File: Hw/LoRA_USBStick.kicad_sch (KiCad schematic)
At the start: 37 parts, among them J10 USB_B, J4 SWD, SW1 RST, SW2 BOOT, SW3 RST, U1 RP2040, U2 RFM95W-868S2, U3 AP2112K-3.3, U4 W25Q16JV, Y1 12Mhz

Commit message: change button for jumper force jumper
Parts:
- removed R1: 1K, Resistor_SMD:R_0603_1608Metric, symbol Device:R_Small
- removed SW2: BOOT, Button_Switch_SMD:SW_SPST_TL3342, symbol Switch:SW_Push
- added JP?: BOOT, symbol Jumper:Jumper_2_Open
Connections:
- net GND: now also JP?.1 (A)
- net QSPI_CS: now also JP?.2 (B)
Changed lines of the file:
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@@
-    (stroke (width 0) (type default) (color 0 0 0 0))
-  )
-  (wire (pts (xy 63.119 129.54) (xy 66.675 129.54))
     (stroke (width 0) (type default) (color 0 0 0 0))
   )
@@
     (stroke (width 0) (type default) (color 0 0 0 0))
   )
-  (wire (pts (xy 50.038 129.54) (xy 50.038 130.556))
+  (wire (pts (xy 55.118 113.03) (xy 55.118 114.046))
     (stroke (width 0) (type default) (color 0 0 0 0))
   )
@@
     (stroke (width 0) (type default) (color 0 0 0 0))
   )
-  (wire (pts (xy 71.755 129.54) (xy 80.01 129.54))
+  (wire (pts (xy 68.199 113.03) (xy 76.454 113.03))
     (stroke (width 0) (type default) (color 0 0 0 0))
   )
@@
     (stroke (width 0) (type default) (color 0 0 0 0))
   )
-  (wire (pts (xy 52.959 129.54) (xy 50.038 129.54))
+  (wire (pts (xy 58.039 113.03) (xy 55.118 113.03))
     (stroke (width 0) (type default) (color 0 0 0 0))
   )
@@
     (effects (font (size 1.27 1.27)) (justify right bottom))
   )
-  (label "QSPI_CS" (at 80.01 129.54 0)
+  (label "QSPI_CS" (at 76.454 113.03 0)
     (effects (font (size 1.27 1.27)) (justify left bottom))
   )
@@
     (pin "2")
   )
-  (symbol (lib_id "Device:R_Small") (at 69.215 129.54 270) (unit 1)
-    (in_bom yes) (on_board yes)
-    (property "Reference" "R1" (id 0) (at 69.215 124.5616 90))
-    (property "Value" "1K" (id 1) (at 69.215 126.873 90))
-    (property "Footprint" "Resistor_SMD:R_0603_1608Metric" (id 2) (at 69.215 129.54 0)
-      (effects (font (size 1.27 1.27)) hide)
-    )
-    (property "Datasheet" "https://lcsc.com/product-detail/Chip-Resistor-Surface-Mount_Walsin-Tech-Corp-Walsin-Tech-Corp-1KR-102-5_C384390.html" (id 3) (at 69.215 129.54 0)
-      (effects (font (size 1.27 1.27)) hide)
-    )
-    (property "LCSC#" "" (id 4) (at 69.215 129.54 0)
-      (effects (font (size 1.27 1.27)) hide)
-    )
-    (property "manf#" "" (id 5) (at 69.215 129.54 0)
-      (effects (font (size 1.27 1.27)) hide)
-    )
-    (pin "1")
-    (pin "2")
-  )
   (symbol (lib_id "power:+1V2") (at 116.332 144.018 0) (unit 1)
     (in_bom yes) (on_board yes)
@@
     (pin "1")
   )
-  (symbol (lib_id "power:GND") (at 50.038 130.556 0) (unit 1)
-    (in_bom yes) (on_board yes)
-    (property "Reference" "#PWR02" (id 0) (at 50.038 136.906 0)
-      (effects (font (size 1.27 1.27)) hide)
-    )
-    (property "Value" "GND" (id 1) (at 50.165 134.9502 0))
-    (property "Footprint" "" (id 2) (at 50.038 130.556 0)
-      (effects (font (size 1.27 1.27)) hide)
-    )
-    (property "Datasheet" "" (id 3) (at 50.038 130.556 0)
+  (symbol (lib_id "power:GND") (at 55.118 114.046 0) (unit 1)
+    (in_bom yes) (on_board yes)
+    (property "Reference" "#PWR02" (id 0) (at 55.118 120.396 0)
+      (effects (font (size 1.27 1.27)) hide)
+    )
+    (property "Value" "GND" (id 1) (at 55.245 118.4402 0))
+    (property "Footprint" "" (id 2) (at 55.118 114.046 0)
+      (effects (font (size 1.27 1.27)) hide)
+    )
+    (property "Datasheet" "" (id 3) (at 55.118 114.046 0)
       (effects (font (size 1.27 1.27)) hide)
     )
@@
     (pin "1")
   )
-  (symbol (lib_id "Switch:SW_Push") (at 58.039 129.54 0) (unit 1)
-    (in_bom yes) (on_board yes)
-    (property "Reference" "SW2" (id 0) (at 58.039 122.301 0))
-    (property "Value" "BOOT" (id 1) (at 58.039 124.6124 0))
-    (property "Footprint" "Button_Switch_SMD:SW_SPST_TL3342" (id 2) (at 58.039 124.46 0)
-      (effects (font (size 1.27 1.27)) hide)
-    )
-    (property "Datasheet" "https://lcsc.com/product-detail/Tactile-Switches_XUNPU-TS-1088R-02526_C455281.html" (id 3) (at 58.039 124.46 0)
-      (effects (font (size 1.27 1.27)) hide)
-    )
-    (property "LCSC#" "" (id 4) (at 58.039 129.54 0)
-      (effects (font (size 1.27 1.27)) hide)
-    )
-    (property "manf#" "TS-1088R-02526" (id 5) (at 58.039 129.54 0)
-      (effects (font (size 1.27 1.27)) hide)
-    )
-    (pin "1")
-    (pin "2")
-  )
   (symbol (lib_id "Device:C_Small") (at 140.97 147.828 0) (unit 1)
     (in_bom yes) (on_board yes)
@@
     )
     (pin "1")
+  )
+  (symbol (lib_id "Jumper:Jumper_2_Open") (at 63.119 113.03 0) (unit 1)
+    (in_bom yes) (on_board yes) (fields_autoplaced)
+    (property "Reference" "JP?" (id 0) (at 63.119 106.68 0))
+    (property "Value" "BOOT" (id 1) (at 63.119 109.22 0))
+    (property "Footprint" "" (id 2) (at 63.119 113.03 0)
+      (effects (font (size 1.27 1.27)) hide)
+    )
+    (property "Datasheet" "~" (id 3) (at 63.119 113.03 0)
+      (effects (font (size 1.27 1.27)) hide)
+    )
+    (pin "1")
+    (pin "2")
   )
   (symbol (lib_id "power:+3V3") (at 155.956 144.272 0) (unit 1)
@@
       (reference "J10") (unit 1) (value "USB_B") (footprint "Connectors:C46394")
     )
-    (path "/73f553b6-40ee-427d-ad00-5afb150dad9e"
-      (reference "R1") (unit 1) (value "1K") (footprint "Resistor_SMD:R_0603_1608Metric")
+    (path "/d9378caf-b15d-41bb-9a08-9c338c99bca0"
+      (reference "JP?") (unit 1) (value "BOOT") (footprint "")
     )
     (path "/f60959af-078b-4b94-af6b-240a70c175cf"
@@
       (reference "SW1") (unit 1) (value "RST") (footprint "Button_Switch_SMD:SW_SPST_TL3342")
     )
-    (path "/9de120ec-a78c-4e0b-898c-8bcfaa48c96b"
-      (reference "SW2") (unit 1) (value "BOOT") (footprint "Button_Switch_SMD:SW_SPST_TL3342")
-    )
     (path "/bd279f0b-459f-41ba-8171-ac9414a30ac1"

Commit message: Place footprints on the PCB
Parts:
- removed SW1: RST, Button_Switch_SMD:SW_SPST_TL3342, symbol LoRA_USBStick-rescue:SW_Push
- JP1: renamed from JP?; footprint (none) -> Jumper:SolderJumper-2_P1.3mm_Open_Pad1.0x1.5mm
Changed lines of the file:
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@@
-    (stroke (width 0) (type default) (color 0 0 0 0))
-  )
-  (wire (pts (xy 163.83 173.99) (xy 163.83 176.53))
     (stroke (width 0) (type default) (color 0 0 0 0))
   )
@@
   )
   (polyline (pts (xy 63.881 197.993) (xy 63.881 166.116))
-    (stroke (width 0) (type default) (color 0 0 0 0))
-  )
-  (wire (pts (xy 163.83 187.833) (xy 163.83 186.69))
     (stroke (width 0) (type default) (color 0 0 0 0))
   )
@@
     (effects (font (size 1.27 1.27)) (justify left bottom))
   )
-  (label "RST" (at 163.83 173.99 0)
-    (effects (font (size 1.524 1.524)) (justify left bottom))
-  )
   (label "MISO" (at 233.68 29.21 180)
     (effects (font (size 1.524 1.524)) (justify right bottom))
@@
   (label "QSPI_DATA3" (at 268.732 148.59 0)
     (effects (font (size 1.27 1.27)) (justify left bottom))
-  )
-  (symbol (lib_id "LoRA_USBStick-rescue:SW_Push") (at 163.83 181.61 270) (unit 1)
-    (in_bom yes) (on_board yes)
-    (property "Reference" "SW1" (id 0) (at 166.37 182.88 0)
-      (effects (font (size 1.27 1.27)) (justify left))
-    )
-    (property "Value" "RST" (id 1) (at 162.306 181.61 0))
-    (property "Footprint" "Button_Switch_SMD:SW_SPST_TL3342" (id 2) (at 168.91 181.61 0)
-      (effects (font (size 1.27 1.27)) hide)
-    )
-    (property "Datasheet" "" (id 3) (at 168.91 181.61 0)
-      (effects (font (size 1.27 1.27)) hide)
-    )
-    (property "manf#" "B3U-1000P" (id 4) (at 163.83 181.61 0)
-      (effects (font (size 1.524 1.524)) hide)
-    )
-    (pin "1")
-    (pin "2")
-  )
-  (symbol (lib_id "power:GND") (at 163.83 187.833 0) (unit 1)
-    (in_bom yes) (on_board yes)
-    (property "Reference" "#PWR01" (id 0) (at 163.83 194.183 0)
-      (effects (font (size 1.27 1.27)) hide)
-    )
-    (property "Value" "GND" (id 1) (at 163.83 191.643 0))
-    (property "Footprint" "" (id 2) (at 163.83 187.833 0)
-      (effects (font (size 1.27 1.27)) hide)
-    )
-    (property "Datasheet" "" (id 3) (at 163.83 187.833 0)
-      (effects (font (size 1.27 1.27)) hide)
-    )
-    (pin "1")
   )
   (symbol (lib_id "power:+3.3V") (at 270.129 25.908 0) (unit 1)
@@
   (symbol (lib_id "power:+3V3") (at 142.24 173.736 0) (unit 1)
     (in_bom yes) (on_board yes)
-    (property "Reference" "#PWR?" (id 0) (at 142.24 177.546 0)
+    (property "Reference" "#PWR0101" (id 0) (at 142.24 177.546 0)
       (effects (font (size 1.27 1.27)) hide)
     )
@@
   (symbol (lib_id "power:GND") (at 140.208 187.325 0) (unit 1)
     (in_bom yes) (on_board yes)
-    (property "Reference" "#PWR?" (id 0) (at 140.208 193.675 0)
+    (property "Reference" "#PWR0102" (id 0) (at 140.208 193.675 0)
       (effects (font (size 1.27 1.27)) hide)
     )
@@
   (symbol (lib_id "Jumper:Jumper_2_Open") (at 63.119 113.03 0) (unit 1)
     (in_bom yes) (on_board yes) (fields_autoplaced)
-    (property "Reference" "JP?" (id 0) (at 63.119 106.68 0))
+    (property "Reference" "JP1" (id 0) (at 63.119 106.68 0))
     (property "Value" "BOOT" (id 1) (at 63.119 109.22 0))
-    (property "Footprint" "" (id 2) (at 63.119 113.03 0)
+    (property "Footprint" "Jumper:SolderJumper-2_P1.3mm_Open_Pad1.0x1.5mm" (id 2) (at 63.119 113.03 0)
       (effects (font (size 1.27 1.27)) hide)
     )
@@
   )
   (symbol_instances
-    (path "/00000000-0000-0000-0000-00005ae4bbf8"
-      (reference "#PWR01") (unit 1) (value "GND") (footprint "")
-    )
     (path "/98cce9f8-8131-4462-bc8b-bd7b4a579405"
       (reference "#PWR02") (unit 1) (value "GND") (footprint "")
@@
     )
     (path "/24088d74-4964-4661-8abf-71a100aa1a44"
-      (reference "#PWR?") (unit 1) (value "+3V3") (footprint "")
+      (reference "#PWR0101") (unit 1) (value "+3V3") (footprint "")
     )
     (path "/cbc339a4-c9ad-4f29-afcf-8e7d53f29096"
-      (reference "#PWR?") (unit 1) (value "GND") (footprint "")
+      (reference "#PWR0102") (unit 1) (value "GND") (footprint "")
     )
     (path "/00000000-0000-0000-0000-00005b06dd9b"
@@
     )
     (path "/d9378caf-b15d-41bb-9a08-9c338c99bca0"
-      (reference "JP?") (unit 1) (value "BOOT") (footprint "")
+      (reference "JP1") (unit 1) (value "BOOT") (footprint "Jumper:SolderJumper-2_P1.3mm_Open_Pad1.0x1.5mm")
     )
     (path "/f60959af-078b-4b94-af6b-240a70c175cf"
@@
       (reference "R11") (unit 1) (value "120R") (footprint "Resistor_SMD:R_0805_2012Metric_Pad1.15x1.40mm_HandSolder")
     )
-    (path "/00000000-0000-0000-0000-00005ae4bb13"
-      (reference "SW1") (unit 1) (value "RST") (footprint "Button_Switch_SMD:SW_SPST_TL3342")
-    )
     (path "/bd279f0b-459f-41ba-8171-ac9414a30ac1"

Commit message: add footprint memory flash
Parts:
- U4: footprint Package_SO:SOIC-8_5.275x5.275mm_P1.27mm -> RP2040:W25Q16JVUUIQ
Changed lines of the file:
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@@
     (property "Reference" "U4" (id 0) (at 245.872 134.366 0))
     (property "Value" "W25Q16JV" (id 1) (at 260.096 134.112 0))
-    (property "Footprint" "Package_SO:SOIC-8_5.275x5.275mm_P1.27mm" (id 2) (at 252.73 143.51 0)
+    (property "Footprint" "RP2040:W25Q16JVUUIQ" (id 2) (at 252.73 143.51 0)
       (effects (font (size 1.27 1.27)) hide)
     )
@@
     )
     (path "/fadc1c63-6a60-4896-9b12-60b8b11e379e"
-      (reference "U4") (unit 1) (value "W25Q16JV") (footprint "Package_SO:SOIC-8_5.275x5.275mm_P1.27mm")
+      (reference "U4") (unit 1) (value "W25Q16JV") (footprint "RP2040:W25Q16JVUUIQ")
     )
     (path "/14b1cf47-fbe7-4d12-9fae-81e256db3a7b"

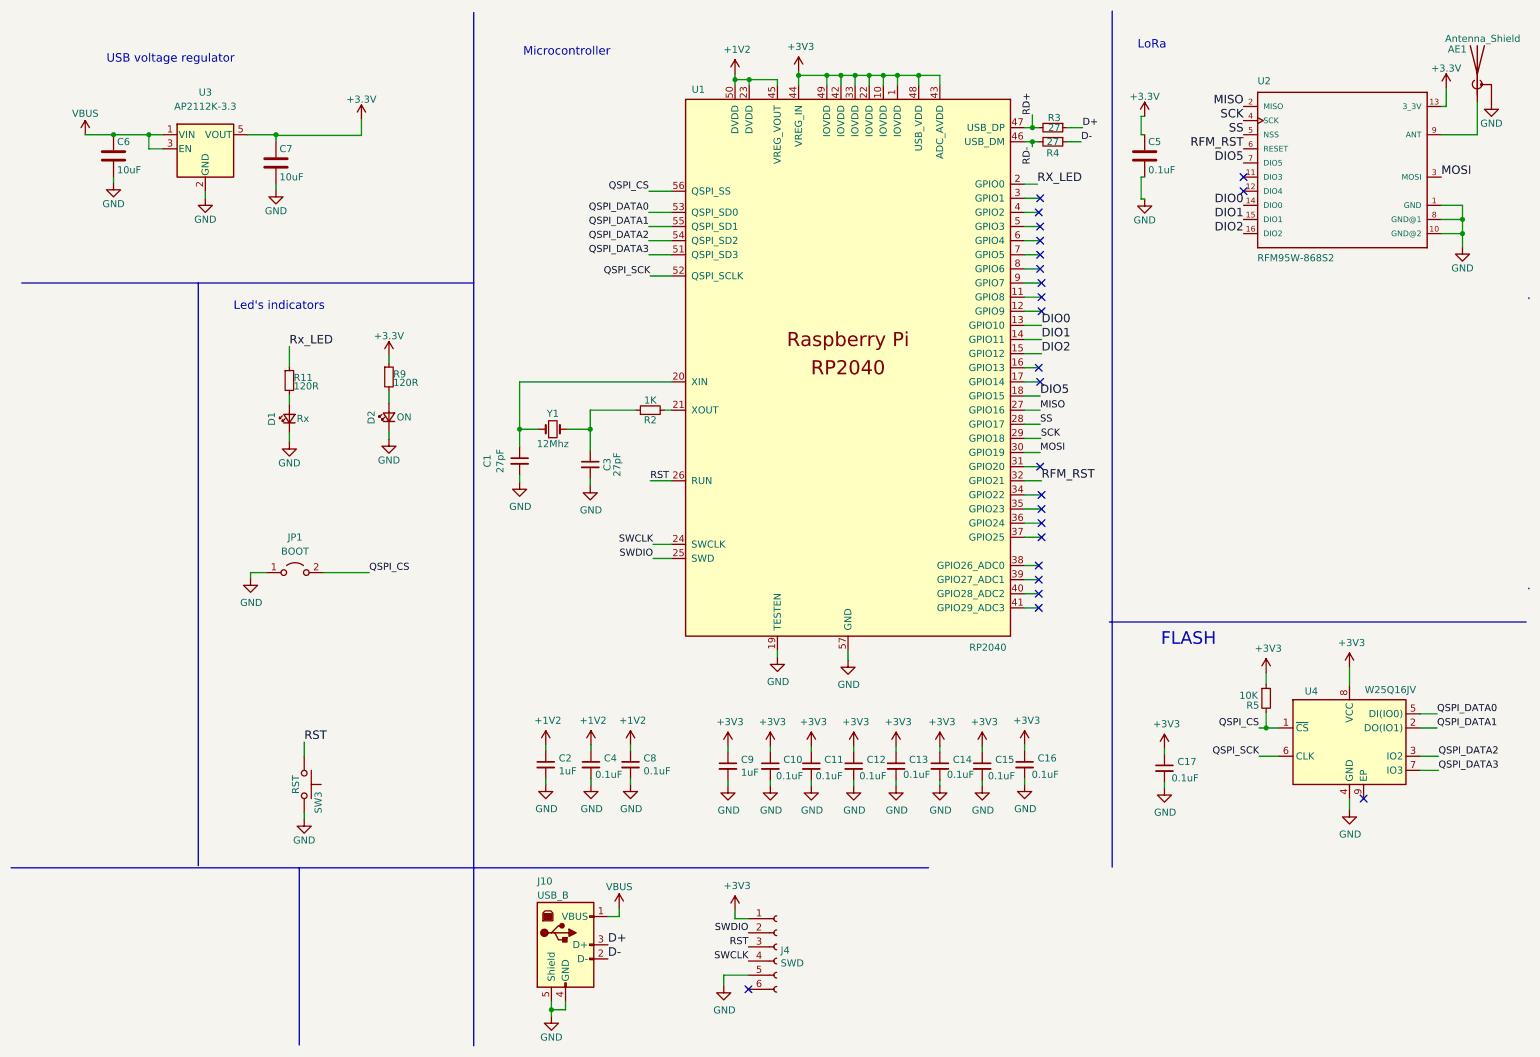
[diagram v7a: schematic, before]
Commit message: New floor plan
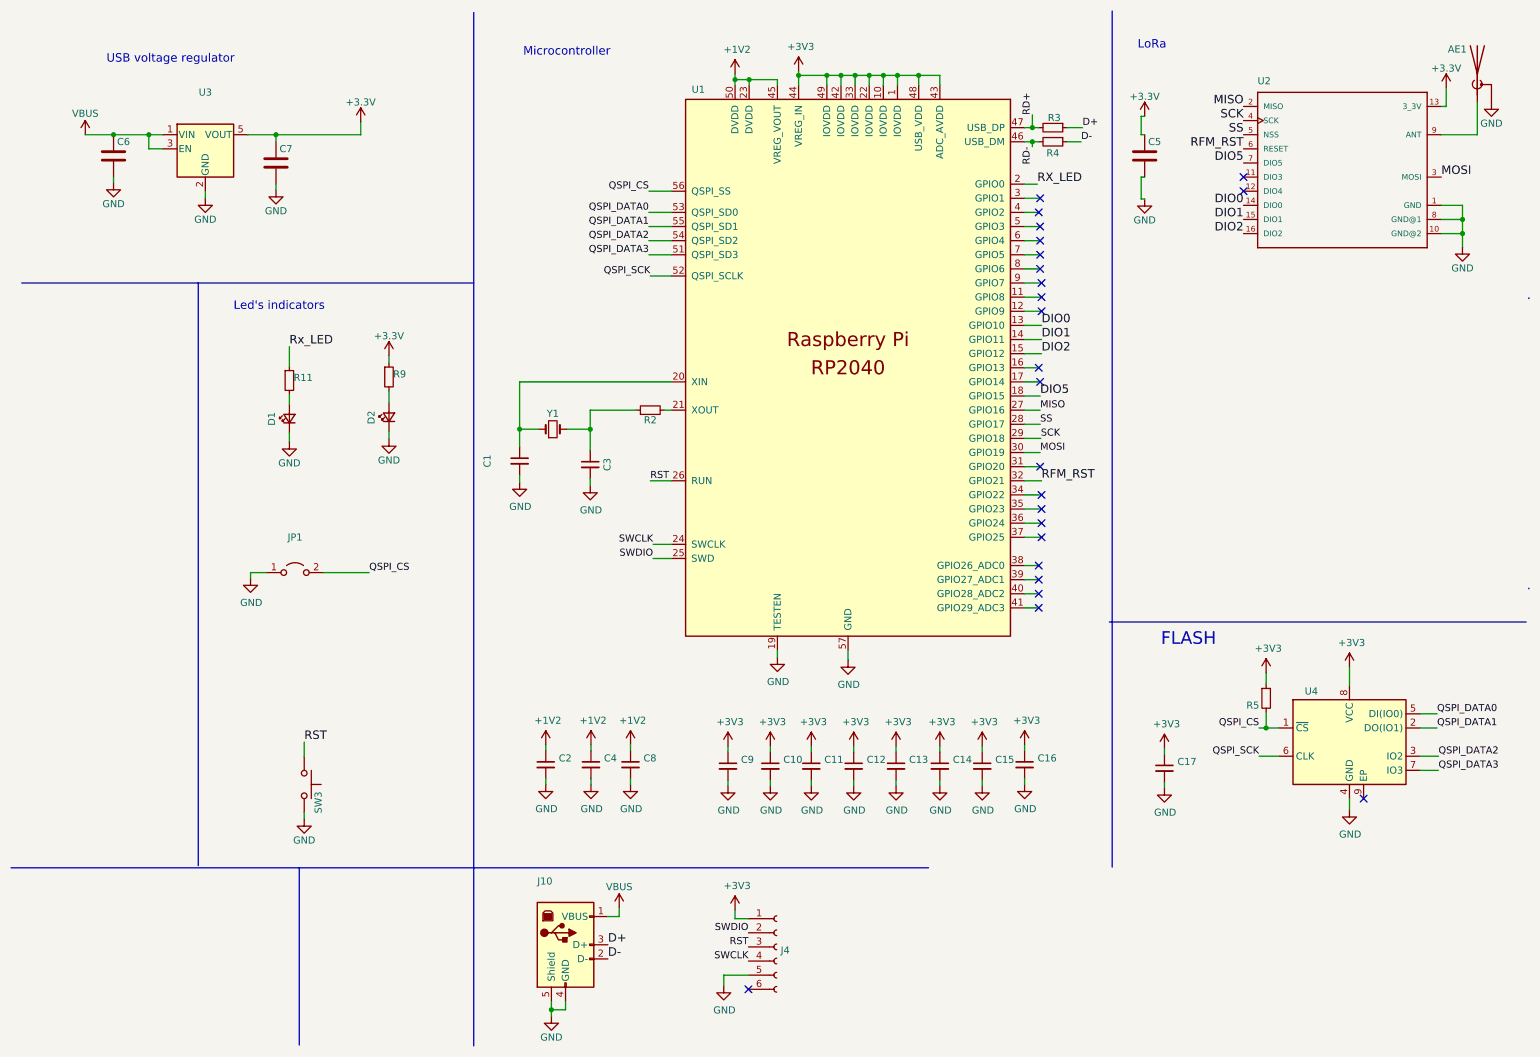
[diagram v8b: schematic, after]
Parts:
- AE1: value Antenna_Shield -> (none); footprint agroin:SMA_EDGE -> (none)
- C1, C3: value 27pF -> (none); footprint Capacitor_SMD:C_0603_1608Metric -> (none)
- C10, C11, C12, C13, C14, C15, C16, C17, C4, C8: value 0.1uF -> (none); footprint Capacitor_SMD:C_0603_1608Metric -> (none)
- C2, C9: value 1uF -> (none); footprint Capacitor_SMD:C_0603_1608Metric -> (none)
- C5: value 0.1uF -> (none); footprint Capacitor_SMD:C_0805_2012Metric_Pad1.15x1.40mm_HandSolder -> (none)
- C6, C7: value 10uF -> (none); footprint Capacitor_SMD:C_0805_2012Metric_Pad1.15x1.40mm_HandSolder -> (none)
- D1: value Rx -> (none); footprint LED_SMD:LED_0805_2012Metric_Pad1.15x1.40mm_HandSolder -> (none)
- D2: value ON -> (none); footprint LED_SMD:LED_0805_2012Metric_Pad1.15x1.40mm_HandSolder -> (none)
- J10: value USB_B -> (none); footprint Connectors:C46394 -> (none)
- J4: value SWD -> (none); footprint Connector:Tag-Connect_TC2030-IDC-NL_2x03_P1.27mm_Vertical -> (none)
- JP1: value BOOT -> (none); footprint Jumper:SolderJumper-2_P1.3mm_Open_Pad1.0x1.5mm -> (none)
- R11, R9: value 120R -> (none); footprint Resistor_SMD:R_0805_2012Metric_Pad1.15x1.40mm_HandSolder -> (none)
- R2: value 1K -> (none); footprint Resistor_SMD:R_0603_1608Metric -> (none)
- R3, R4: value 27 -> (none); footprint Resistor_SMD:R_0603_1608Metric -> (none)
- R5: value 10K -> (none); footprint Resistor_SMD:R_0603_1608Metric -> (none)
- SW3: value RST -> (none); footprint Button_Switch_SMD:SW_SPST_TL3342 -> (none)
- U1: value RP2040 -> (none); footprint RP2040:RP2040-QFN-56 -> (none)
- U2: value RFM95W-868S2 -> (none); footprint RF_Module:HOPERF_RFM9XW_SMD -> (none)
- U3: value AP2112K-3.3 -> (none); footprint Package_TO_SOT_SMD:SOT-23-5 -> (none)
- U4: value W25Q16JV -> (none); footprint RP2040:W25Q16JVUUIQ -> (none)
- Y1: value 12Mhz -> (none); footprint Crystal:Crystal_SMD_5032-2Pin_5.0x3.2mm -> (none)
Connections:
- net +3V3: now also U3.5 (VOUT)
